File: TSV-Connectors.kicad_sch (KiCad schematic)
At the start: 3 parts, among them J3 DTF13-4P-G003, J5 DTF13-4P-G003, J6 1053091104

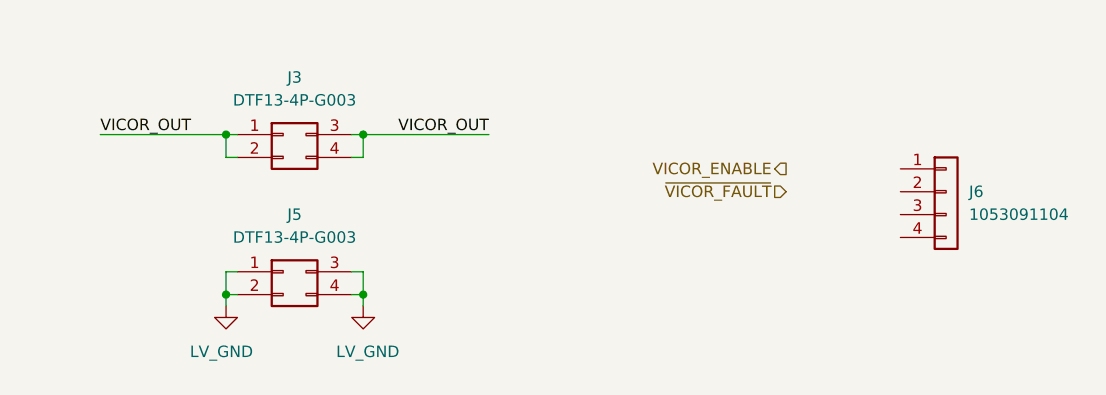
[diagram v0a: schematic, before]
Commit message: Finished up draft 1 of schematic
Need to look everything over and do a quick layout
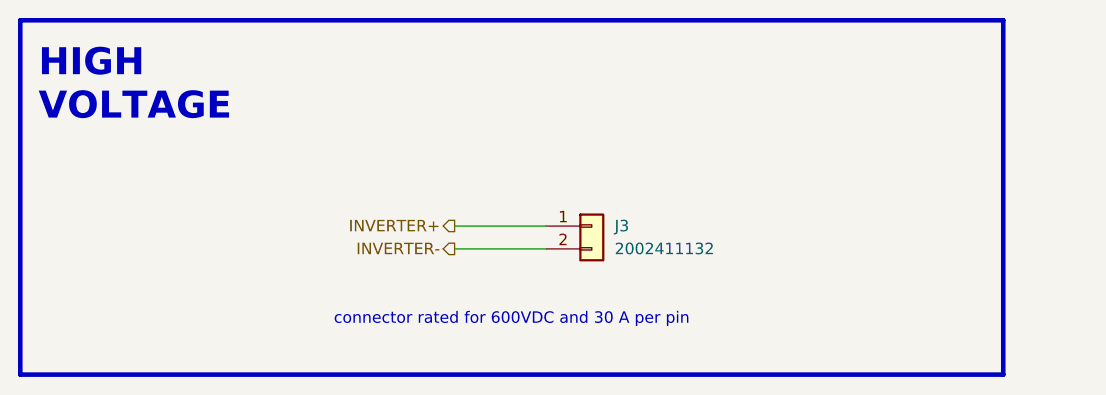
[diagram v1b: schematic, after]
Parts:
- removed J3, J5: DTF13-4P-G003, AERO_Connectors:DTF13-4P-G003, symbol AERO_Connectors:DTF13-4P-G003
- removed J6: 1053091104, AERO_Connectors:1053091104, symbol AERO_Connectors:1053091104
- added J3: 2002411132, AERO_Connectors:2002411132, symbol AERO_Connectors:2002411132
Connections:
- new net INVERTER+: J3.1 (Pin_1)
- new net INVERTER-: J3.2 (Pin_2)
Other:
- note added: "HIGH VOLTAGE"
- note added: "connector rated for 600VDC and 30 A per pin"

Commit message: Started layout
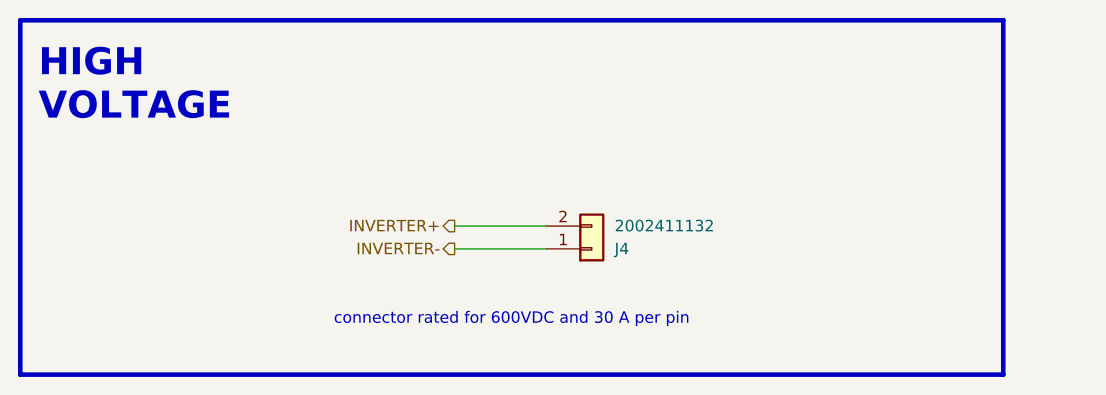
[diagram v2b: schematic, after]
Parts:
- renumbered J3 to J4
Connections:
- net INVERTER+: now also J4.2 (Pin_2); no longer J4.1 (Pin_1)
- net INVERTER-: now also J4.1 (Pin_1); no longer J4.2 (Pin_2)
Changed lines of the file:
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@@
 	(wire
 		(pts
-			(xy 134.62 107.95) (xy 144.78 107.95)
+			(xy 134.62 105.41) (xy 144.78 105.41)
 		)
 		(stroke
@@
 	(wire
 		(pts
-			(xy 134.62 105.41) (xy 144.78 105.41)
+			(xy 134.62 107.95) (xy 144.78 107.95)
 		)
 		(stroke
@@
 	(symbol
 		(lib_id "AERO_Connectors:2002411132")
-		(at 149.86 105.41 0)
+		(at 149.86 107.95 0)
+		(mirror x)
 		(unit 1)
 		(body_style 1)
@@
 		(in_pos_files yes)
 		(dnp no)
-		(fields_autoplaced yes)
-		(property "Reference" "J3"
-			(at 152.4 105.4099 0)
+		(property "Reference" "J4"
+			(at 152.4 107.9501 0)
 			(show_name no)
 			(do_not_autoplace no)
@@
 		)
 		(property "Value" "2002411132"
-			(at 152.4 107.9499 0)
+			(at 152.4 105.4101 0)
 			(show_name no)
 			(do_not_autoplace no)
@@
 		)
 		(property "Footprint" "AERO_Connectors:2002411132"
-			(at 149.86 105.41 0)
+			(at 149.86 107.95 0)
 			(hide yes)
 			(show_name no)
@@
 		)
 		(property "Datasheet" "https://www.molex.com/en-us/products/part-detail/2002411132?display=pdf"
-			(at 149.86 105.41 0)
+			(at 149.86 107.95 0)
 			(hide yes)
 			(show_name no)
@@
 		)
 		(property "Description" "molex mega fit, male, single row, 01x02,"
-			(at 149.86 105.41 0)
+			(at 149.86 107.95 0)
 			(hide yes)
 			(show_name no)
@@
 			(project "Blinky"
 				(path "/63c9e8ce-1f6e-4570-90a7-b8c1c309328a/e09c43e6-d1ac-424f-8f6f-b32a45a91117"
-					(reference "J3")
+					(reference "J4")
 					(unit 1)
 				)
